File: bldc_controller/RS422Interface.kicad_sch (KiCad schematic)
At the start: 2 parts, among them U5 SN65HVD35DR

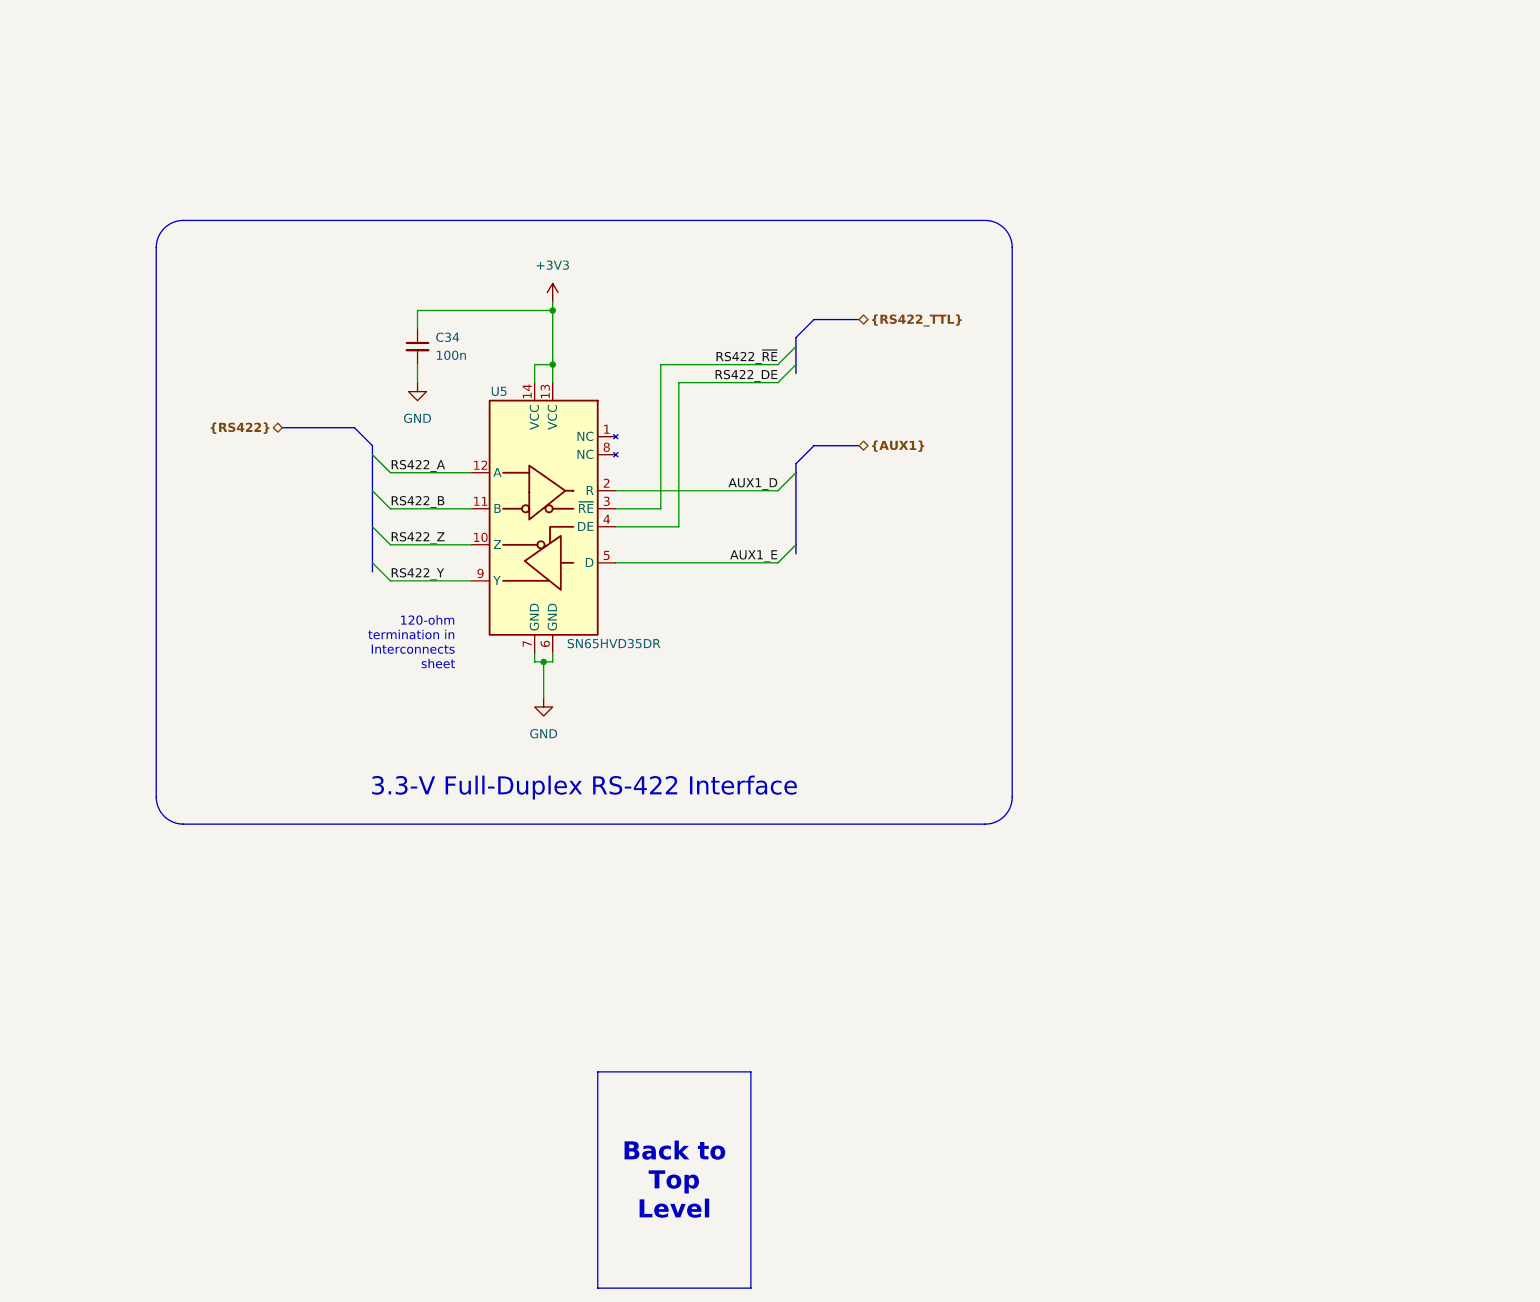
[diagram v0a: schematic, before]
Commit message: added temporary footprints and deleted extra files
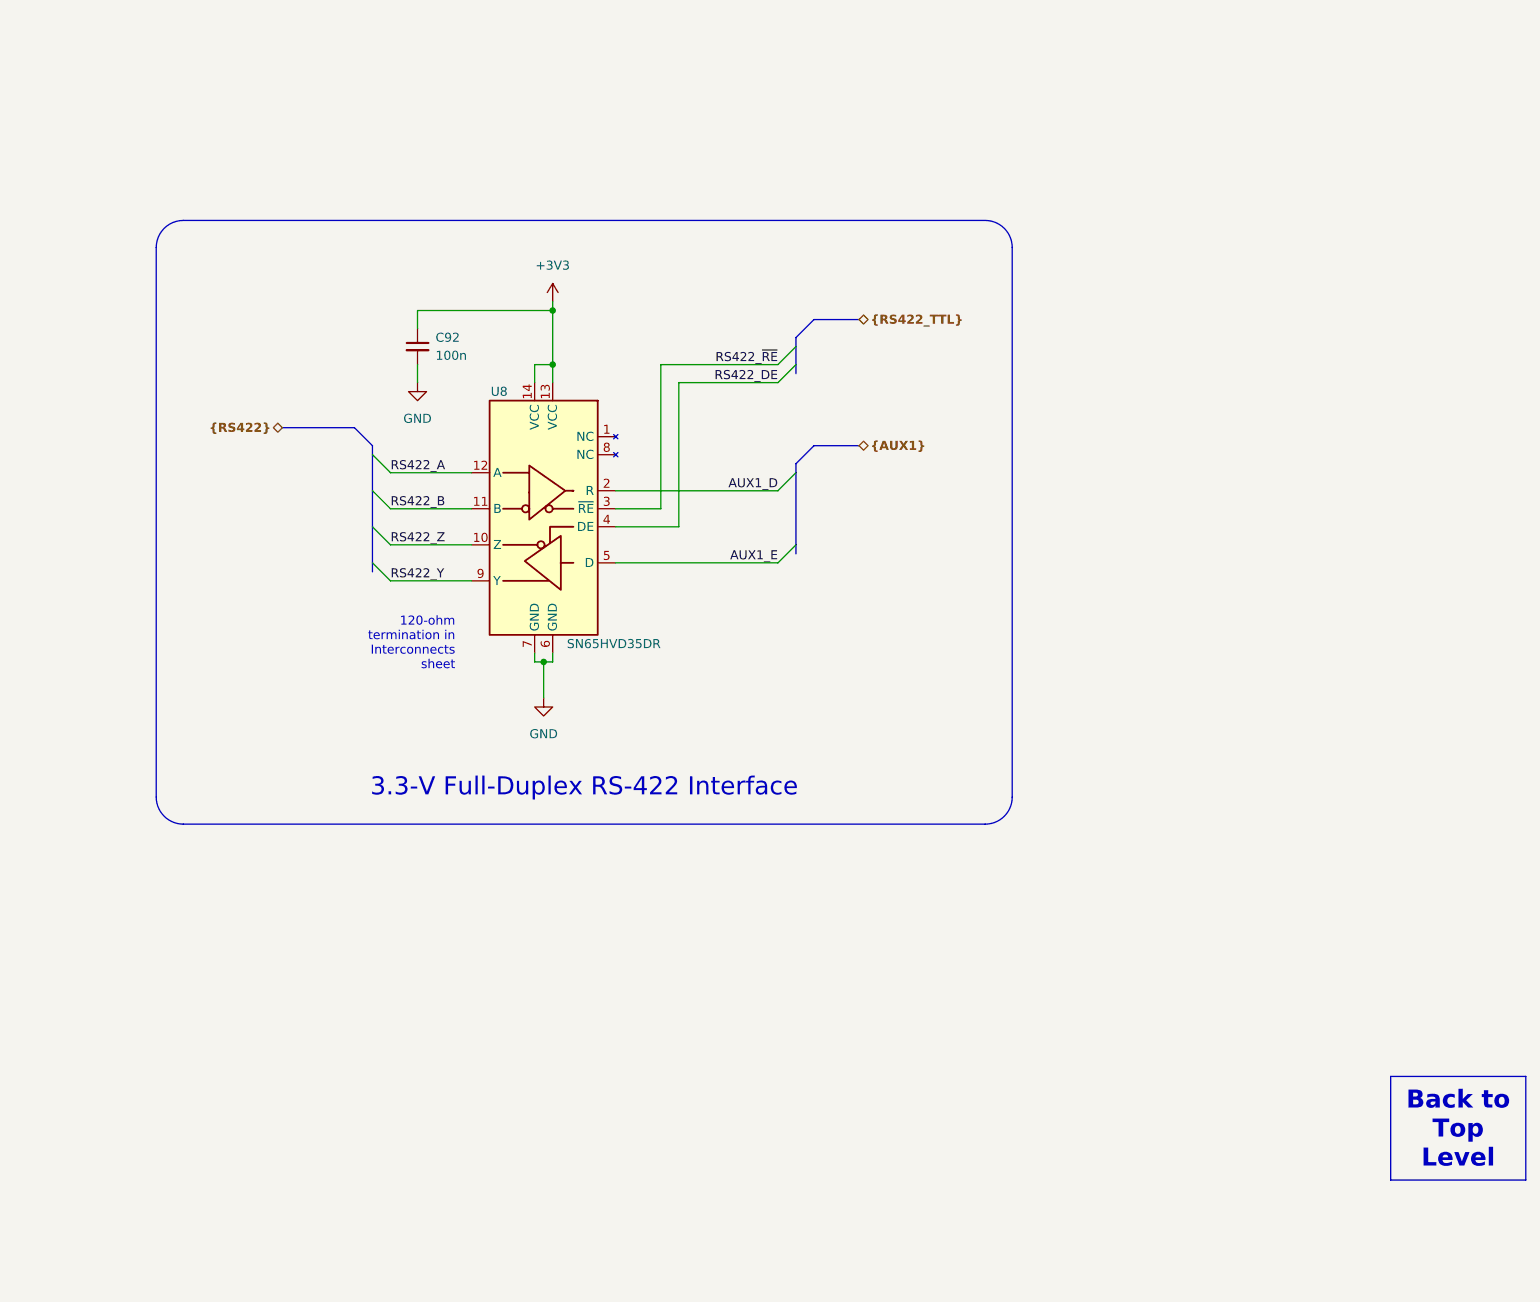
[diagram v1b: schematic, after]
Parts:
- C92: renamed from C34; footprint (none) -> Capacitor_SMD:C_0402_1005Metric
- renumbered U5 to U8
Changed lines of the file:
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@@
     (fill (type none))
-  )
-  (text_box "Back to Top Level"
-    (at 153.67 165.735 0) (size 21.59 30.48)
-    (stroke (width 0) (type default) (color 0 0 0 1))
-    (fill (type color) (color 0 0 0 0.1))
-    (effects (font (size 2.54 2.54) (thickness 0.508) bold (color 0 0 0 1)) (href "#1"))
   )
   (text_box "120-ohm termination in Interconnects sheet"
@@
     (fill (type none))
     (effects (font (size 2.54 2.54) (color 0 0 0 1)) (justify bottom))
+  )
+  (text_box "Back to Top Level"
+    (at 265.43 166.37 0) (size 19.05 14.605)
+    (stroke (width 0) (type default) (color 0 0 0 1))
+    (fill (type color) (color 0 0 0 0.1))
+    (effects (font (size 2.54 2.54) (thickness 0.508) bold (color 0 0 0 1)) (href "#1"))
   )
   (label "RS422_~{RE}" (at 179.07 66.04 180) (fields_autoplaced)
@@
     (effects (font (size 1.27 1.27)) (justify left bottom))
   )
-  (hierarchical_label "{RS422_TTL}" (shape bidirectional) (at 190.5 59.69 0) (fields_autoplaced)
-    (effects (font (size 1.27 1.27) bold) (justify left))
+  (hierarchical_label "{RS422}" (shape bidirectional) (at 109.22 74.93 180) (fields_autoplaced)
+    (effects (font (size 1.27 1.27) bold) (justify right))
   )
   (hierarchical_label "{AUX1}" (shape bidirectional) (at 190.5 77.47 0) (fields_autoplaced)
     (effects (font (size 1.27 1.27) bold) (justify left))
   )
-  (hierarchical_label "{RS422}" (shape bidirectional) (at 109.22 74.93 180) (fields_autoplaced)
-    (effects (font (size 1.27 1.27) bold) (justify right))
+  (hierarchical_label "{RS422_TTL}" (shape bidirectional) (at 190.5 59.69 0) (fields_autoplaced)
+    (effects (font (size 1.27 1.27) bold) (justify left))
   )
   (symbol (lib_id "power:+3V3") (at 147.32 57.15 0) (unit 1)
     (in_bom yes) (on_board yes) (dnp no) (fields_autoplaced)
-    (property "Reference" "#PWR047" (at 147.32 60.96 0)
+    (property "Reference" "#PWR052" (at 147.32 60.96 0)
       (effects (font (size 1.27 1.27)) hide)
     )
@@
       (project "bldc_controller"
         (path "/0650c7a8-acba-429c-9f8e-eec0baf0bc1c/50cb6c1b-2a97-41f7-b806-2f324483583f"
-          (reference "#PWR047") (unit 1)
+          (reference "#PWR052") (unit 1)
         )
       )
@@
   (symbol (lib_id "Device:C_Small") (at 128.27 63.5 0) (unit 1)
     (in_bom yes) (on_board yes) (dnp no) (fields_autoplaced)
-    (property "Reference" "C34" (at 130.81 62.2363 0)
+    (property "Reference" "C92" (at 130.81 62.2363 0)
       (effects (font (size 1.27 1.27)) (justify left))
     )
@@
       (effects (font (size 1.27 1.27)) (justify left))
     )
-    (property "Footprint" "" (at 128.27 63.5 0)
+    (property "Footprint" "Capacitor_SMD:C_0402_1005Metric" (at 128.27 63.5 0)
       (effects (font (size 1.27 1.27)) hide)
     )
@@
       (project "bldc_controller"
         (path "/0650c7a8-acba-429c-9f8e-eec0baf0bc1c/50cb6c1b-2a97-41f7-b806-2f324483583f"
-          (reference "C34") (unit 1)
+          (reference "C92") (unit 1)
         )
       )
@@
   (symbol (lib_id "power:GND") (at 128.27 68.58 0) (unit 1)
     (in_bom yes) (on_board yes) (dnp no) (fields_autoplaced)
-    (property "Reference" "#PWR048" (at 128.27 74.93 0)
+    (property "Reference" "#PWR050" (at 128.27 74.93 0)
       (effects (font (size 1.27 1.27)) hide)
     )
@@
       (project "bldc_controller"
         (path "/0650c7a8-acba-429c-9f8e-eec0baf0bc1c/50cb6c1b-2a97-41f7-b806-2f324483583f"
-          (reference "#PWR048") (unit 1)
+          (reference "#PWR050") (unit 1)
         )
       )
@@
   (symbol (lib_id "power:GND") (at 146.05 113.03 0) (unit 1)
     (in_bom yes) (on_board yes) (dnp no) (fields_autoplaced)
-    (property "Reference" "#PWR049" (at 146.05 119.38 0)
+    (property "Reference" "#PWR051" (at 146.05 119.38 0)
       (effects (font (size 1.27 1.27)) hide)
     )
@@
       (project "bldc_controller"
         (path "/0650c7a8-acba-429c-9f8e-eec0baf0bc1c/50cb6c1b-2a97-41f7-b806-2f324483583f"
-          (reference "#PWR049") (unit 1)
+          (reference "#PWR051") (unit 1)
         )
       )
@@
   (symbol (lib_id "0_interface_uart:SN65HVD35DR") (at 146.05 88.9 0) (mirror y) (unit 1)
     (in_bom yes) (on_board yes) (dnp no)
-    (property "Reference" "U5" (at 140.97 69.85 0)
+    (property "Reference" "U8" (at 140.97 69.85 0)
       (effects (font (size 1.27 1.27)) (justify left))
     )
@@
       (project "bldc_controller"
         (path "/0650c7a8-acba-429c-9f8e-eec0baf0bc1c/50cb6c1b-2a97-41f7-b806-2f324483583f"
-          (reference "U5") (unit 1)
+          (reference "U8") (unit 1)
         )
       )

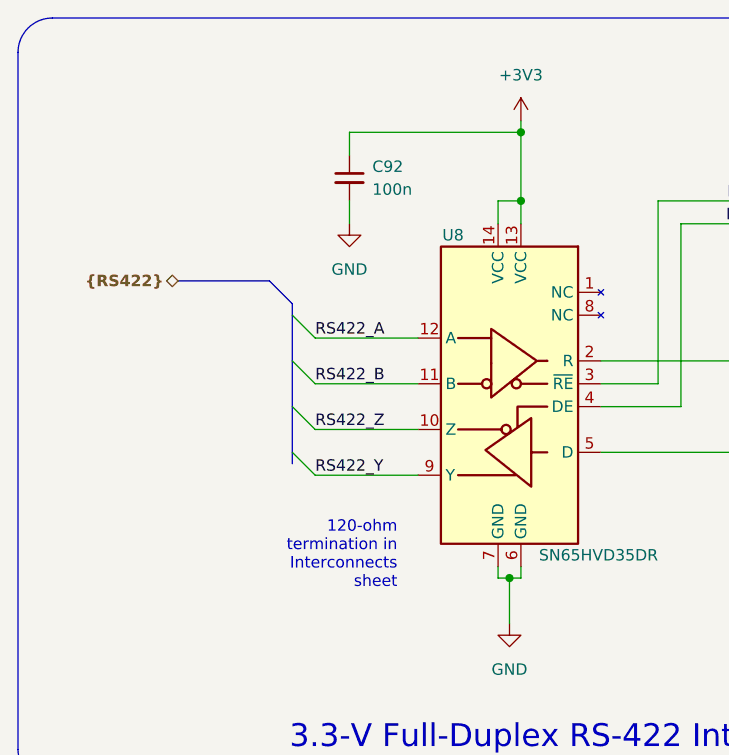
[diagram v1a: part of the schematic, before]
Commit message: added IPC-7351 compliant footprints and started routing
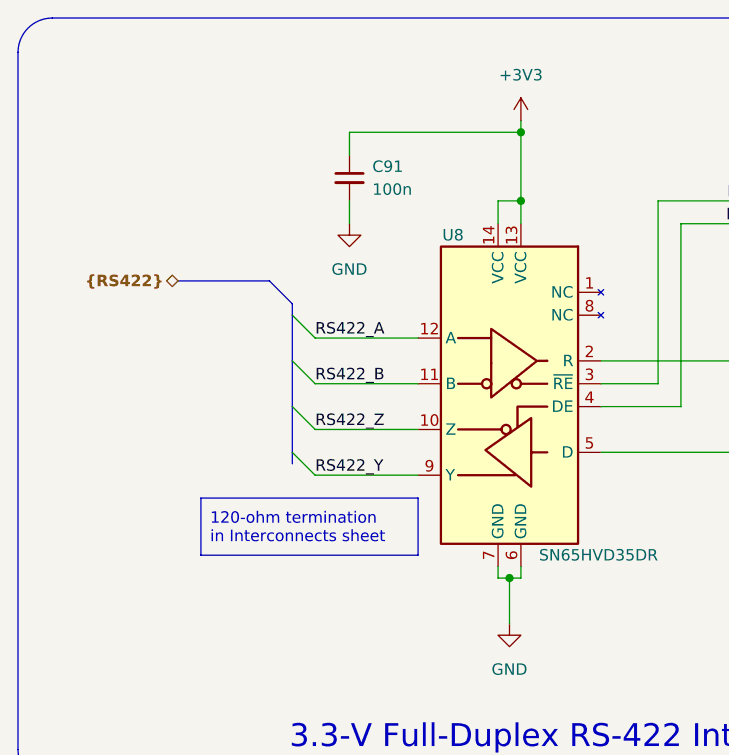
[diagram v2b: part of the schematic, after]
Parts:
- C91: renamed from C92; footprint Capacitor_SMD:C_0402_1005Metric -> 0_capacitor_smd:C_0402_1005_DensityHigh
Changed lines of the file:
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@@
   )
   (text_box "120-ohm termination in Interconnects sheet"
-    (at 115.57 100.33 0) (size 19.05 10.16)
-    (stroke (width -0.0001) (type default))
-    (fill (type none))
-    (effects (font (size 1.27 1.27)) (justify right top))
+    (at 111.76 99.06 0) (size 24.13 6.35)
+    (stroke (width 0) (type default) (color 0 0 0 1))
+    (fill (type color) (color 191 240 255 1))
+    (effects (font (size 1.27 1.27) (color 0 0 0 1)) (justify left))
   )
   (text_box "3.3-V Full-Duplex RS-422 Interface"
@@
   (symbol (lib_id "power:+3V3") (at 147.32 57.15 0) (unit 1)
     (in_bom yes) (on_board yes) (dnp no) (fields_autoplaced)
-    (property "Reference" "#PWR052" (at 147.32 60.96 0)
+    (property "Reference" "#PWR051" (at 147.32 60.96 0)
       (effects (font (size 1.27 1.27)) hide)
     )
@@
       (project "bldc_controller"
         (path "/0650c7a8-acba-429c-9f8e-eec0baf0bc1c/50cb6c1b-2a97-41f7-b806-2f324483583f"
-          (reference "#PWR052") (unit 1)
+          (reference "#PWR051") (unit 1)
         )
       )
@@
   (symbol (lib_id "Device:C_Small") (at 128.27 63.5 0) (unit 1)
     (in_bom yes) (on_board yes) (dnp no) (fields_autoplaced)
-    (property "Reference" "C92" (at 130.81 62.2363 0)
+    (property "Reference" "C91" (at 130.81 62.2363 0)
       (effects (font (size 1.27 1.27)) (justify left))
     )
@@
       (effects (font (size 1.27 1.27)) (justify left))
     )
-    (property "Footprint" "Capacitor_SMD:C_0402_1005Metric" (at 128.27 63.5 0)
+    (property "Footprint" "0_capacitor_smd:C_0402_1005_DensityHigh" (at 128.27 63.5 0)
       (effects (font (size 1.27 1.27)) hide)
     )
@@
       (project "bldc_controller"
         (path "/0650c7a8-acba-429c-9f8e-eec0baf0bc1c/50cb6c1b-2a97-41f7-b806-2f324483583f"
-          (reference "C92") (unit 1)
+          (reference "C91") (unit 1)
         )
       )
@@
   (symbol (lib_id "power:GND") (at 128.27 68.58 0) (unit 1)
     (in_bom yes) (on_board yes) (dnp no) (fields_autoplaced)
-    (property "Reference" "#PWR050" (at 128.27 74.93 0)
+    (property "Reference" "#PWR049" (at 128.27 74.93 0)
       (effects (font (size 1.27 1.27)) hide)
     )
@@
       (project "bldc_controller"
         (path "/0650c7a8-acba-429c-9f8e-eec0baf0bc1c/50cb6c1b-2a97-41f7-b806-2f324483583f"
-          (reference "#PWR050") (unit 1)
+          (reference "#PWR049") (unit 1)
         )
       )
@@
   (symbol (lib_id "power:GND") (at 146.05 113.03 0) (unit 1)
     (in_bom yes) (on_board yes) (dnp no) (fields_autoplaced)
-    (property "Reference" "#PWR051" (at 146.05 119.38 0)
+    (property "Reference" "#PWR050" (at 146.05 119.38 0)
       (effects (font (size 1.27 1.27)) hide)
     )
@@
       (project "bldc_controller"
         (path "/0650c7a8-acba-429c-9f8e-eec0baf0bc1c/50cb6c1b-2a97-41f7-b806-2f324483583f"
-          (reference "#PWR051") (unit 1)
+          (reference "#PWR050") (unit 1)
         )
       )

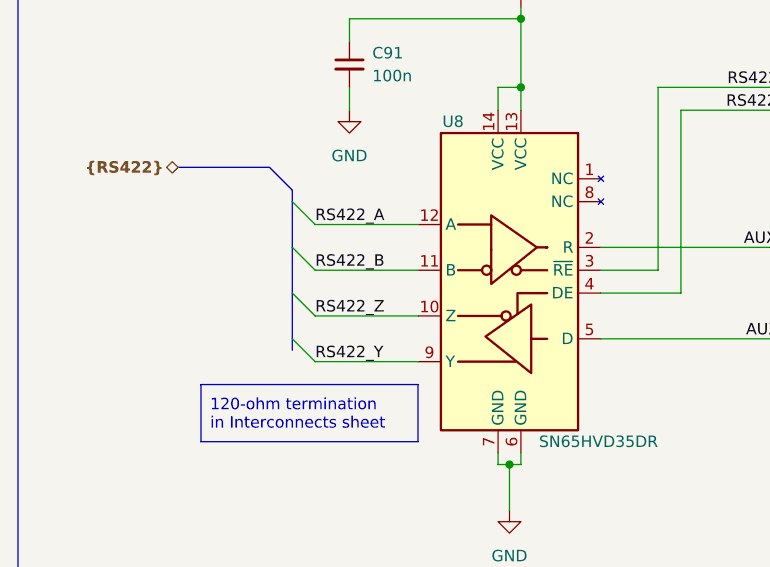
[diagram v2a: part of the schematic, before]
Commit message: routed CAN, added new footprints
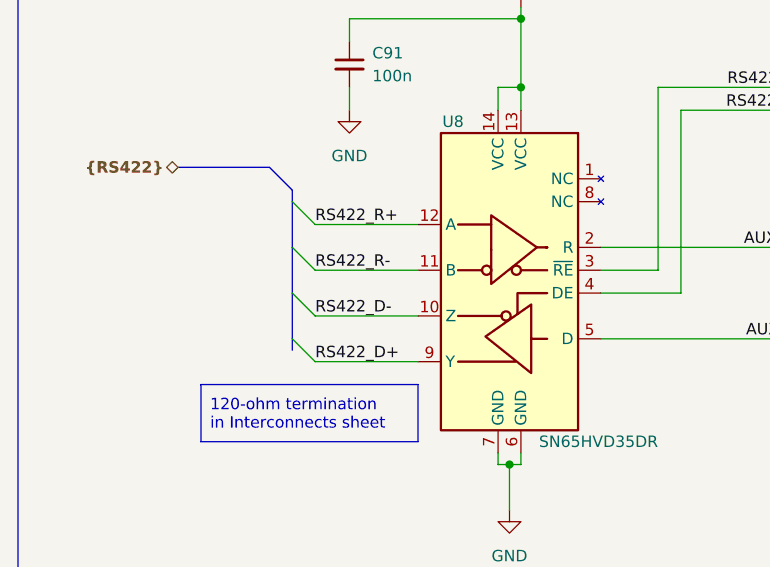
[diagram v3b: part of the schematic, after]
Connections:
- net RS422_A renamed RS422_R+
- net RS422_B renamed RS422_R-
- net RS422_Y renamed RS422_D+
- net RS422_Z renamed RS422_D-
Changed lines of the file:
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@@
     (effects (font (size 1.27 1.27)) (justify right bottom))
   )
-  (label "RS422_Z" (at 124.46 91.44 0) (fields_autoplaced)
+  (label "RS422_D-" (at 124.46 91.44 0) (fields_autoplaced)
     (effects (font (size 1.27 1.27)) (justify left bottom))
   )
-  (label "RS422_Y" (at 124.46 96.52 0) (fields_autoplaced)
+  (label "RS422_D+" (at 124.46 96.52 0) (fields_autoplaced)
     (effects (font (size 1.27 1.27)) (justify left bottom))
   )
-  (label "RS422_A" (at 124.46 81.28 0) (fields_autoplaced)
+  (label "RS422_R+" (at 124.46 81.28 0) (fields_autoplaced)
     (effects (font (size 1.27 1.27)) (justify left bottom))
   )
@@
     (effects (font (size 1.27 1.27)) (justify right bottom))
   )
-  (label "RS422_B" (at 124.46 86.36 0) (fields_autoplaced)
+  (label "RS422_R-" (at 124.46 86.36 0) (fields_autoplaced)
     (effects (font (size 1.27 1.27)) (justify left bottom))
   )
